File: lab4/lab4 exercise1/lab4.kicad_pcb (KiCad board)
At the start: 2 copper layers, 6 parts, among them SW1 s

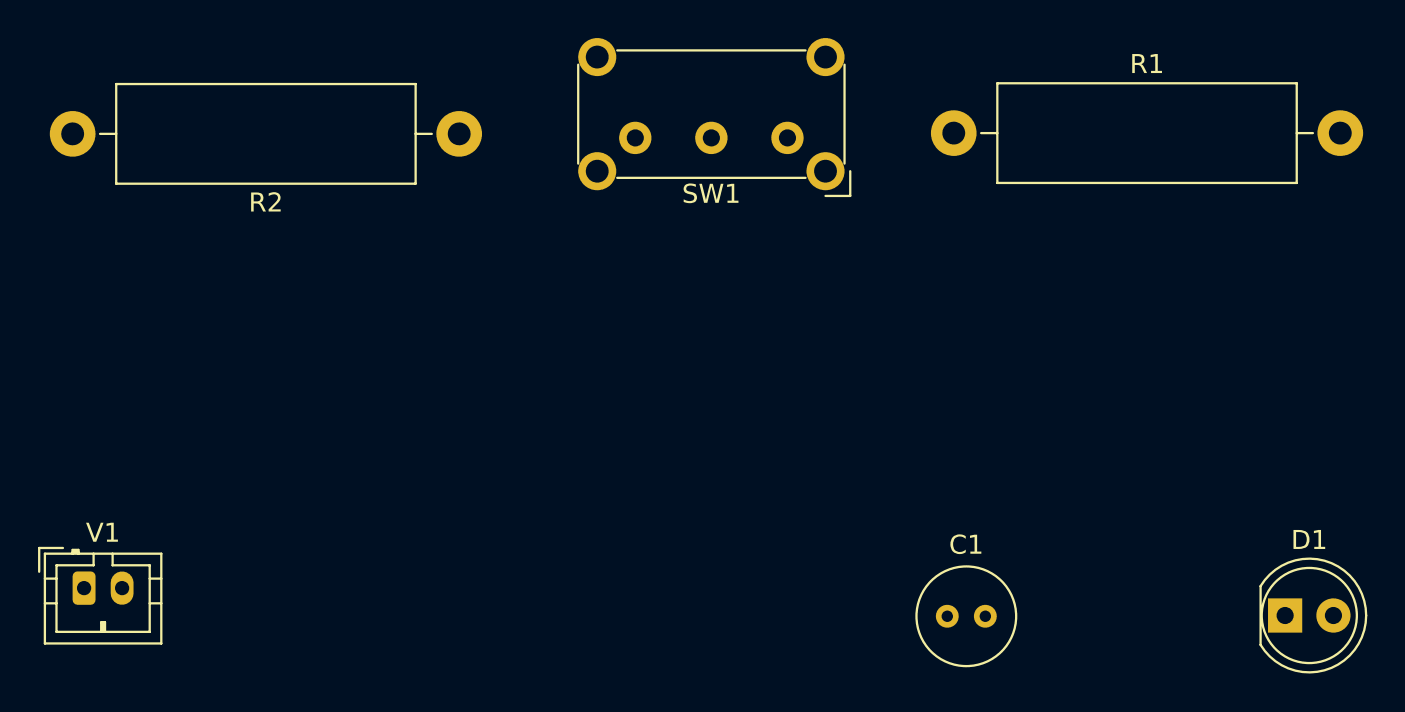
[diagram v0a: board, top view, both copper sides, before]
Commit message: Updated lab 4 pcb layout
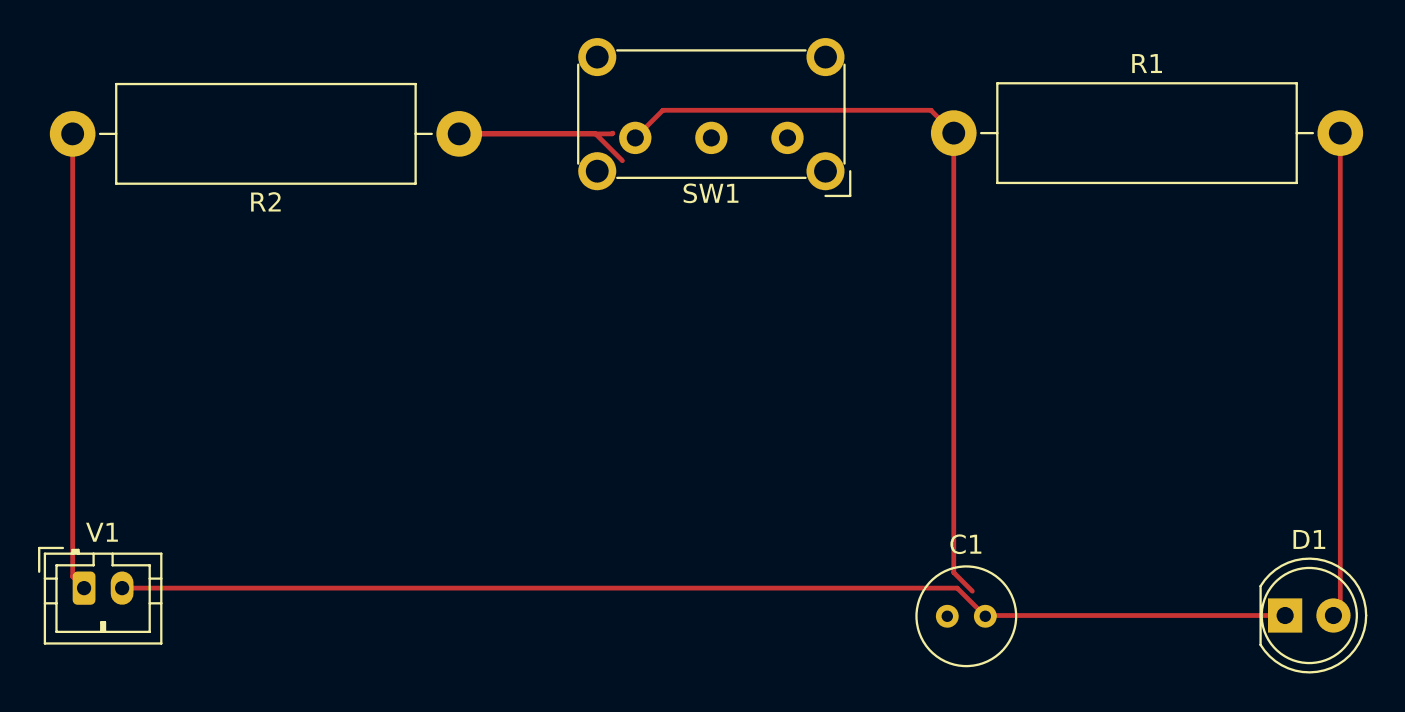
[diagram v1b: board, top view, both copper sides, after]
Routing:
- net Net-(C1-Pad2): track 0.00 -> 61.8 mm
- net Net-(C1-Pad1): track 0.00 -> 42.3 mm
- net Net-(D1-Pad2): track 0.00 -> 25.4 mm
- net Net-(R2-Pad2): track 0.00 -> 24.1 mm
- net Net-(R2-Pad1): track 0.00 -> 17.3 mm
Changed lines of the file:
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@@
     )
   )
+  (segment (start 142.19 69.92) (end 140.7375 71.3725) (width 0.25) (layer "F.Cu") (net 1))
+  (segment (start 156.28 69.92) (end 142.19 69.92) (width 0.25) (layer "F.Cu") (net 1))
+  (segment (start 157.48 71.12) (end 156.28 69.92) (width 0.25) (layer "F.Cu") (net 1))
+  (segment (start 157.48 94.223604) (end 158.458198 95.201802) (width 0.25) (layer "F.Cu") (net 1))
+  (segment (start 157.48 71.12) (end 157.48 94.223604) (width 0.25) (layer "F.Cu") (net 1))
+  (segment (start 157.66 95.04) (end 159.14 96.52) (width 0.25) (layer "F.Cu") (net 2))
+  (segment (start 159.18 96.48) (end 159.14 96.52) (width 0.25) (layer "F.Cu") (net 2))
+  (segment (start 174.9 96.48) (end 159.18 96.48) (width 0.25) (layer "F.Cu") (net 2))
+  (segment (start 113.76 95.04) (end 157.66 95.04) (width 0.25) (layer "F.Cu") (net 2))
+  (segment (start 177.8 71.12) (end 177.8 96.52) (width 0.25) (layer "F.Cu") (net 3))
+  (segment (start 138.648833 71.16) (end 140.0625 72.573667) (width 0.25) (layer "F.Cu") (net 4))
+  (segment (start 131.48 71.16) (end 138.648833 71.16) (width 0.25) (layer "F.Cu") (net 4))
+  (segment (start 139.5225 71.16) (end 139.5625 71.12) (width 0.25) (layer "F.Cu") (net 4))
+  (segment (start 131.48 71.16) (end 139.5225 71.16) (width 0.25) (layer "F.Cu") (net 4))
+  (segment (start 111.16 94.44) (end 111.76 95.04) (width 0.25) (layer "F.Cu") (net 5))
+  (segment (start 111.16 71.16) (end 111.16 94.44) (width 0.25) (layer "F.Cu") (net 5))
 )
